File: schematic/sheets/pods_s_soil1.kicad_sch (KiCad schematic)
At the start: 6 parts, among them M1 PUMP-5V-1A, Q1 IRLZ44N

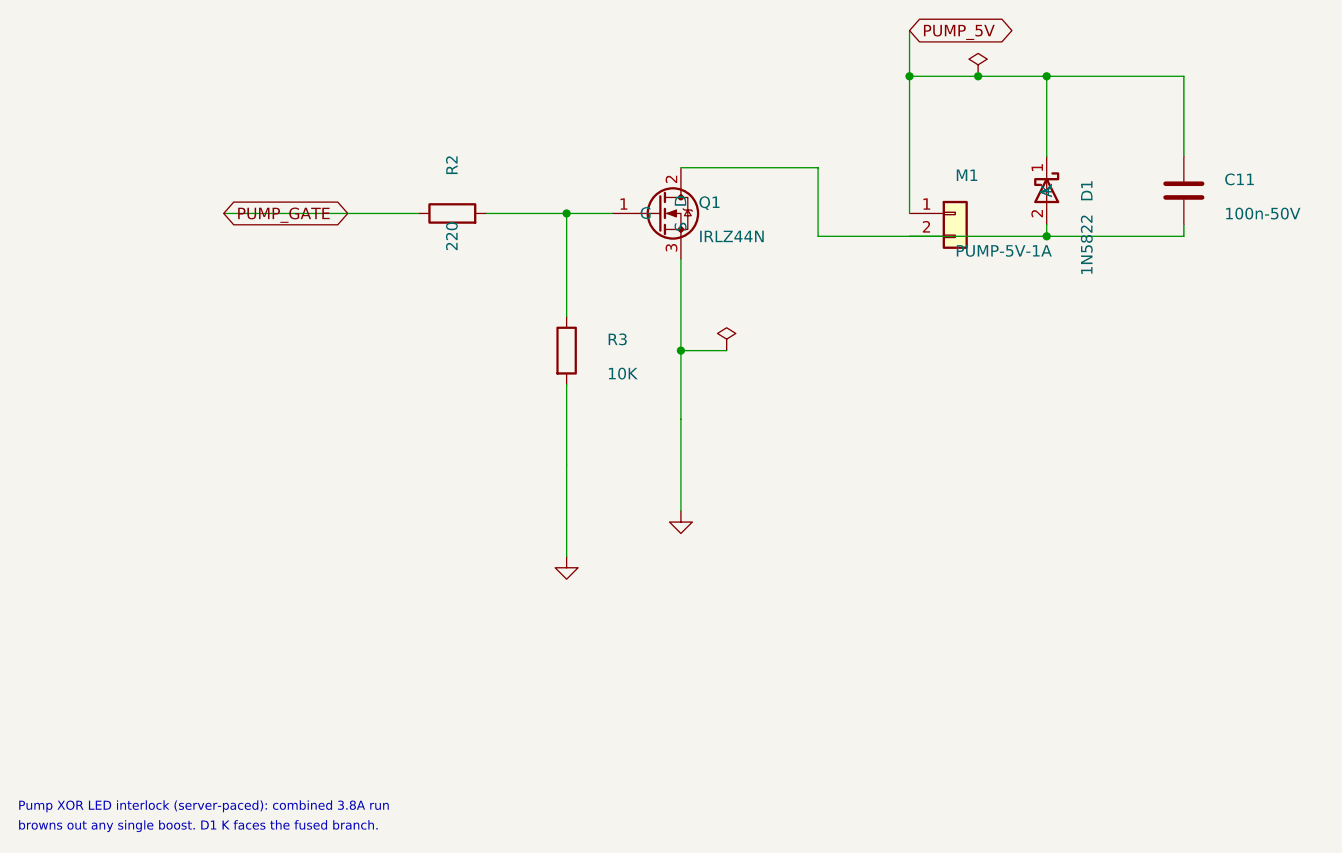
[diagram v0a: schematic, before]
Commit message: Organize schematic/: sheets/ mfg/ final/, drop sklib
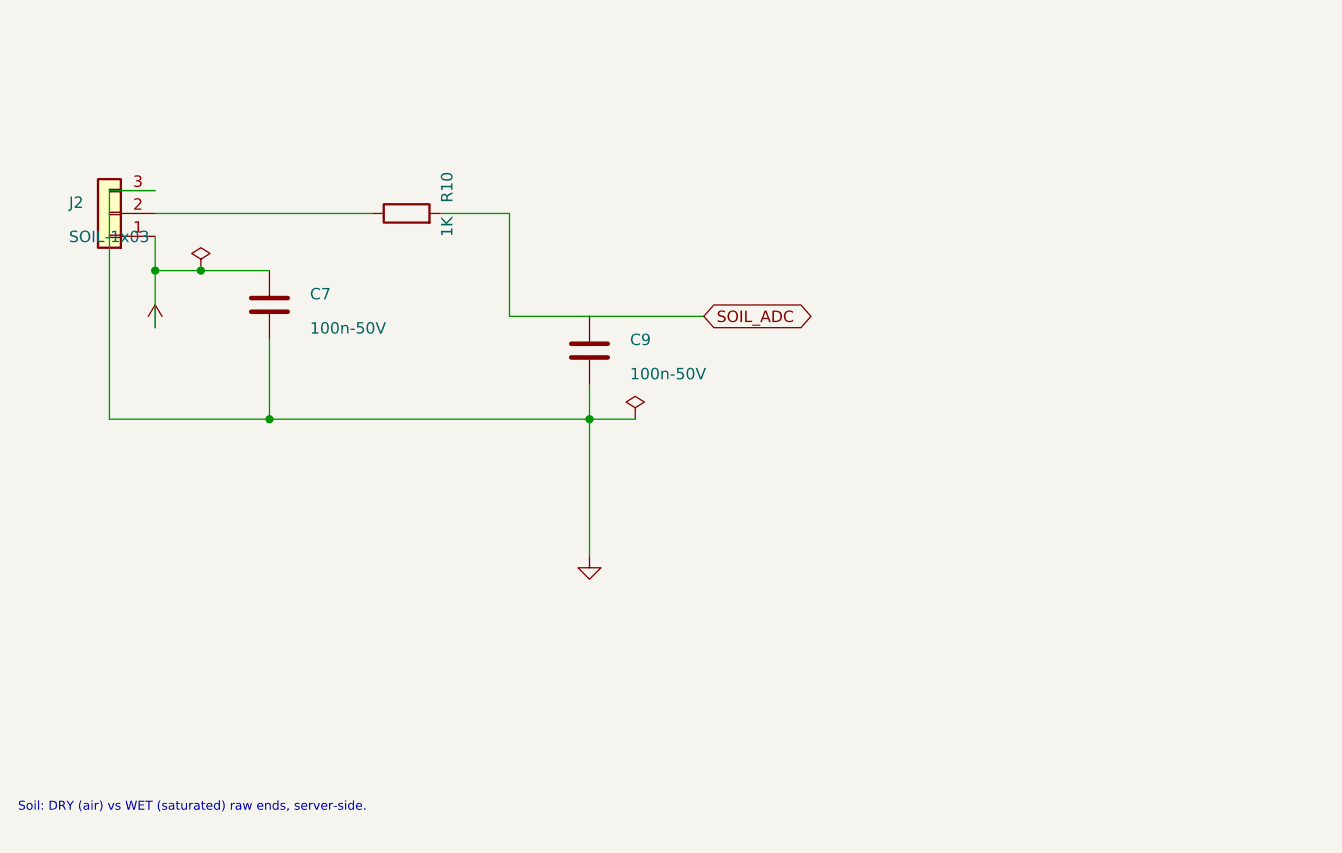
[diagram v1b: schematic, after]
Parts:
- removed C11: 100n-50V, Capacitor_SMD:C_0603_1608Metric, symbol Device:C
- removed D1: 1N5822, Diode_THT:D_DO-41_SOD81_P7.62mm_Horizontal, symbol Diode:1N5819
- removed M1: PUMP-5V-1A, Connector_PinHeader_2.54mm:PinHeader_1x02_P2.54mm_Vertical, symbol Connector_Generic:Conn_01x02
- removed Q1: IRLZ44N, Package_TO_SOT_THT:TO-220-3_Vertical, symbol Transistor_FET:IRLZ44N
- removed R2: 220, Resistor_SMD:R_0603_1608Metric, symbol Device:R
- removed R3: 10K, Resistor_SMD:R_0603_1608Metric, symbol Device:R
- added C7, C9: 100n-50V, Capacitor_SMD:C_0603_1608Metric, symbol Device:C
- added J2: SOIL-1x03, Connector_PinHeader_2.54mm:PinHeader_1x03_P2.54mm_Vertical, symbol Connector_Generic:Conn_01x03
- added R10: 1K, Resistor_SMD:R_0603_1608Metric, symbol Device:R
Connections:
- net GND: now also C7.2, C9.2, J2.3 (Pin_3)
- new net: J2.2 (Pin_2), R10.1
- new net +3V3: C7.1, J2.1 (Pin_1)
- new net SOIL_ADC: C9.1, R10.2
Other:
- note added: "Soil: DRY (air) vs WET (saturated) raw ends, server-side."
- note removed: "Pump XOR LED interlock (server-paced): combined 3.8A run"
- note removed: "browns out any single boost. D1 K faces the fused branch."
